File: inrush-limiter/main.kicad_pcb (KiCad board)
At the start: 2 copper layers, 27 parts, among them K1 RELAY_2RT, P1 CONN_01X04, P2 CONN_01X02, Q1 PN2222A, Q2 PN2222A, U1 LM393

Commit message: fix connections
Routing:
- net Net-(Q1-Pad2): track 0.00 -> 6.88 mm
- net GND: track 138.0 -> 138.8 mm
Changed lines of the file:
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@@
   (general
     (links 46)
-    (no_connects 2)
+    (no_connects 0)
     (area 112.645 37.775 201.022 98.675001)
     (thickness 1.6)
     (drawings 0)
-    (tracks 122)
+    (tracks 127)
     (zones 0)
     (modules 27)
@@
     (pad_to_mask_clearance 0.2)
     (aux_axis_origin 0 0)
-    (visible_elements FFFFFF7F)
+    (visible_elements FFFFFFFF)
     (pcbplotparams
       (layerselection 0x00030_80000001)
@@
   (segment (start 127 90.17) (end 133.35 90.17) (width 0.5) (layer B.Cu) (net 1))
   (segment (start 124.46 83.82) (end 124.46 87.63) (width 0.5) (layer B.Cu) (net 1) (status 30))
+  (segment (start 142.23746 67.30948) (end 147.31746 67.30948) (width 0.5) (layer B.Cu) (net 2))
+  (segment (start 121.92 58.42) (end 121.92 72.39) (width 0.5) (layer B.Cu) (net 2))
+  (segment (start 116.84 72.39) (end 116.84 76.2) (width 0.5) (layer B.Cu) (net 2))
+  (segment (start 118.11 72.39) (end 116.84 72.39) (width 0.5) (layer B.Cu) (net 2))
+  (segment (start 121.92 72.39) (end 118.11 72.39) (width 0.5) (layer B.Cu) (net 2))
   (segment (start 130.81 50.8) (end 121.93 50.8) (width 0.5) (layer B.Cu) (net 2) (status 20))
   (segment (start 130.81 60.96) (end 130.81 50.8) (width 0.5) (layer B.Cu) (net 2))
@@
   (segment (start 121.93 50.8) (end 121.92 50.79) (width 0.5) (layer B.Cu) (net 2) (status 30))
   (segment (start 121.92 50.79) (end 121.92 58.42) (width 0.5) (layer B.Cu) (net 2) (status 30))
-  (segment (start 116.84 74.93) (end 118.11 73.66) (width 0.5) (layer B.Cu) (net 2))
+  (segment (start 116.84 74.93) (end 116.84 76.2) (width 0.5) (layer B.Cu) (net 2))
   (segment (start 119.38 90.13) (end 118.07 90.13) (width 0.5) (layer B.Cu) (net 2) (status 10))
+  (segment (start 116.84 76.2) (end 116.84 88.9) (width 0.5) (layer B.Cu) (net 2))
   (segment (start 116.84 88.9) (end 118.07 90.13) (width 0.5) (layer B.Cu) (net 2))
-  (segment (start 116.84 74.93) (end 116.84 88.9) (width 0.5) (layer B.Cu) (net 2))
-  (segment (start 118.11 73.66) (end 137.16 73.66) (width 0.5) (layer B.Cu) (net 2))
   (segment (start 124.46 95.25) (end 121.92 95.25) (width 0.5) (layer B.Cu) (net 2) (status 10))
   (segment (start 121.92 95.25) (end 119.38 92.71) (width 0.5) (layer B.Cu) (net 2))
   (segment (start 119.38 92.71) (end 119.38 90.13) (width 0.5) (layer B.Cu) (net 2) (status 20))
-  (segment (start 137.16 67.31) (end 137.16 73.66) (width 0.5) (layer B.Cu) (net 2) (status 10))
   (segment (start 142.23746 67.30948) (end 137.16052 67.30948) (width 0.5) (layer B.Cu) (net 2) (status 30))
   (segment (start 137.16052 67.30948) (end 137.16 67.31) (width 0.5) (layer B.Cu) (net 2) (status 30))
@@
   (segment (start 165.1 64.77) (end 165.1 69.85) (width 2) (layer B.Cu) (net 4))
   (segment (start 165.52926 64.34074) (end 165.1 64.77) (width 2) (layer B.Cu) (net 4))
-  (segment (start 121.92 46.99) (end 119.38 49.53) (width 0.5) (layer B.Cu) (net 5) (status 400000))
-  (segment (start 119.38 49.53) (end 119.38 58.42) (width 0.5) (layer B.Cu) (net 5) (status 800000))
-  (segment (start 121.92 46.99) (end 125.73 43.18) (width 0.5) (layer B.Cu) (net 5) (status 400000))
-  (segment (start 125.73 43.18) (end 130.81 43.18) (width 0.5) (layer B.Cu) (net 5) (status 800000))
+  (segment (start 121.92 46.99) (end 119.38 49.53) (width 0.5) (layer B.Cu) (net 5) (status 10))
+  (segment (start 119.38 49.53) (end 119.38 58.42) (width 0.5) (layer B.Cu) (net 5) (status 20))
+  (segment (start 121.92 46.99) (end 125.73 43.18) (width 0.5) (layer B.Cu) (net 5) (status 10))
+  (segment (start 125.73 43.18) (end 130.81 43.18) (width 0.5) (layer B.Cu) (net 5) (status 20))
   (segment (start 137.16254 43.18052) (end 132.08052 43.18052) (width 0.5) (layer B.Cu) (net 5) (status 10))
   (segment (start 132.08052 43.18052) (end 130.81104 43.18) (width 0.5) (layer B.Cu) (net 5) (status 20))
@@
   (segment (start 147.31746 53.33948) (end 147.32 53.33694) (width 0.5) (layer B.Cu) (net 6) (status 30))
   (segment (start 147.32306 53.34) (end 147.32254 53.33948) (width 0.5) (layer B.Cu) (net 6) (status 30))
-  (segment (start 137.16254 53.34052) (end 137.16254 46.99254) (width 0.5) (layer B.Cu) (net 7) (status 400000))
-  (segment (start 135.89 45.72) (end 130.81 45.72) (width 0.5) (layer B.Cu) (net 7) (status 800000))
+  (segment (start 137.16254 53.34052) (end 137.16254 46.99254) (width 0.5) (layer B.Cu) (net 7) (status 10))
+  (segment (start 135.89 45.72) (end 130.81 45.72) (width 0.5) (layer B.Cu) (net 7) (status 20))
   (segment (start 137.16254 46.99254) (end 135.89 45.72) (width 0.5) (layer B.Cu) (net 7))
   (segment (start 137.16 53.33798) (end 137.16254 53.34052) (width 0.5) (layer B.Cu) (net 7) (status 30))
@@
   (segment (start 177.39868 69.85) (end 177.8 70.25132) (width 2) (layer B.Cu) (net 8) (status 30))
   (segment (start 178.20132 69.85) (end 177.8 70.25132) (width 2) (layer B.Cu) (net 8) (status 30))
-  (segment (start 190.5 52.23) (end 171.61 52.23) (width 2) (layer B.Cu) (net 9))
-  (segment (start 171.61 52.23) (end 170.18 50.8) (width 2) (layer B.Cu) (net 9))
+  (segment (start 190.5 52.23) (end 171.61 52.23) (width 2) (layer B.Cu) (net 9) (status 10))
+  (segment (start 171.61 52.23) (end 170.18 50.8) (width 2) (layer B.Cu) (net 9) (status 20))
   (segment (start 190.5 57.23) (end 190.5 52.23) (width 2) (layer B.Cu) (net 9) (status 30))
   (segment (start 190.5 52.23) (end 190.34 52.07) (width 2) (layer B.Cu) (net 9) (status 30))
+  (segment (start 156.21 80.01) (end 154.94 81.28) (width 0.5) (layer B.Cu) (net 10) (status 10))
+  (segment (start 154.94 81.28) (end 154.94 86.36) (width 0.5) (layer B.Cu) (net 10) (status 20))
   (segment (start 130.81 87.63) (end 130.81 83.82) (width 0.5) (layer B.Cu) (net 11) (status 30))
   (segment (start 130.81 83.82) (end 137.16 83.82) (width 0.5) (layer B.Cu) (net 11) (status 30))
@@
   (segment (start 160.02 52.07) (end 163.83 52.07) (width 0.5) (layer B.Cu) (net 17) (status 10))
   (segment (start 163.83 52.07) (end 164.86 51.04) (width 0.5) (layer B.Cu) (net 17) (status 20))
-  (segment (start 190.5 47.23) (end 190.5 46.99) (width 2) (layer B.Cu) (net 18))
-  (segment (start 190.5 46.99) (end 185.84926 42.33926) (width 2) (layer B.Cu) (net 18))
-  (segment (start 185.84926 42.33926) (end 177.8 42.33926) (width 2) (layer B.Cu) (net 18))
+  (segment (start 190.5 47.23) (end 190.5 46.99) (width 2) (layer B.Cu) (net 18) (status 30))
+  (segment (start 190.5 46.99) (end 185.84926 42.33926) (width 2) (layer B.Cu) (net 18) (status 10))
+  (segment (start 185.84926 42.33926) (end 177.8 42.33926) (width 2) (layer B.Cu) (net 18) (status 20))
   (segment (start 177.8 42.33926) (end 178.22926 42.33926) (width 2) (layer B.Cu) (net 18) (status 30))
   (zone (net 2) (net_name GND) (layer B.Cu) (hatch edge 0.508)

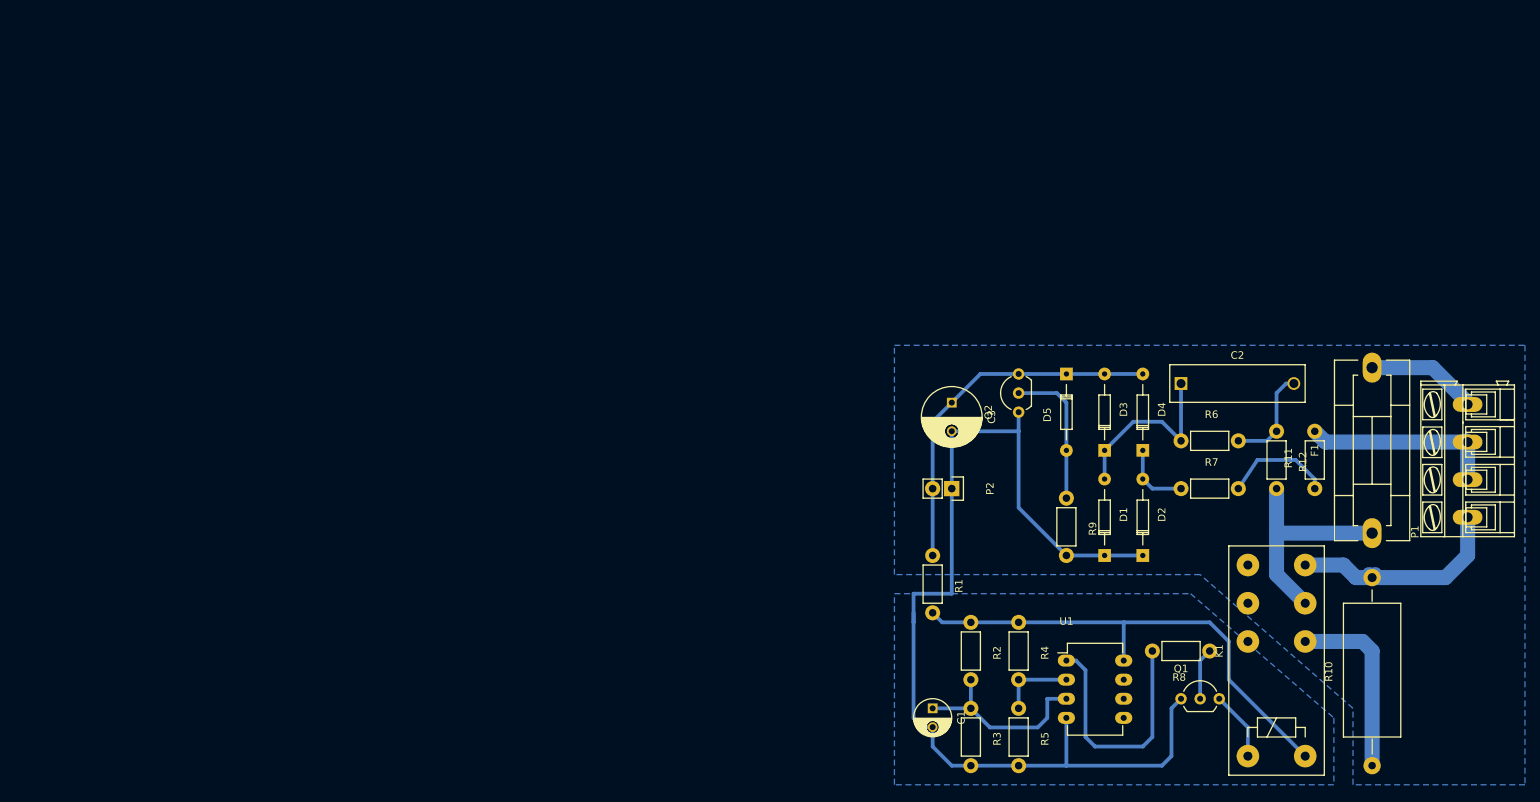
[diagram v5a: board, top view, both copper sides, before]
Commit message: add leds
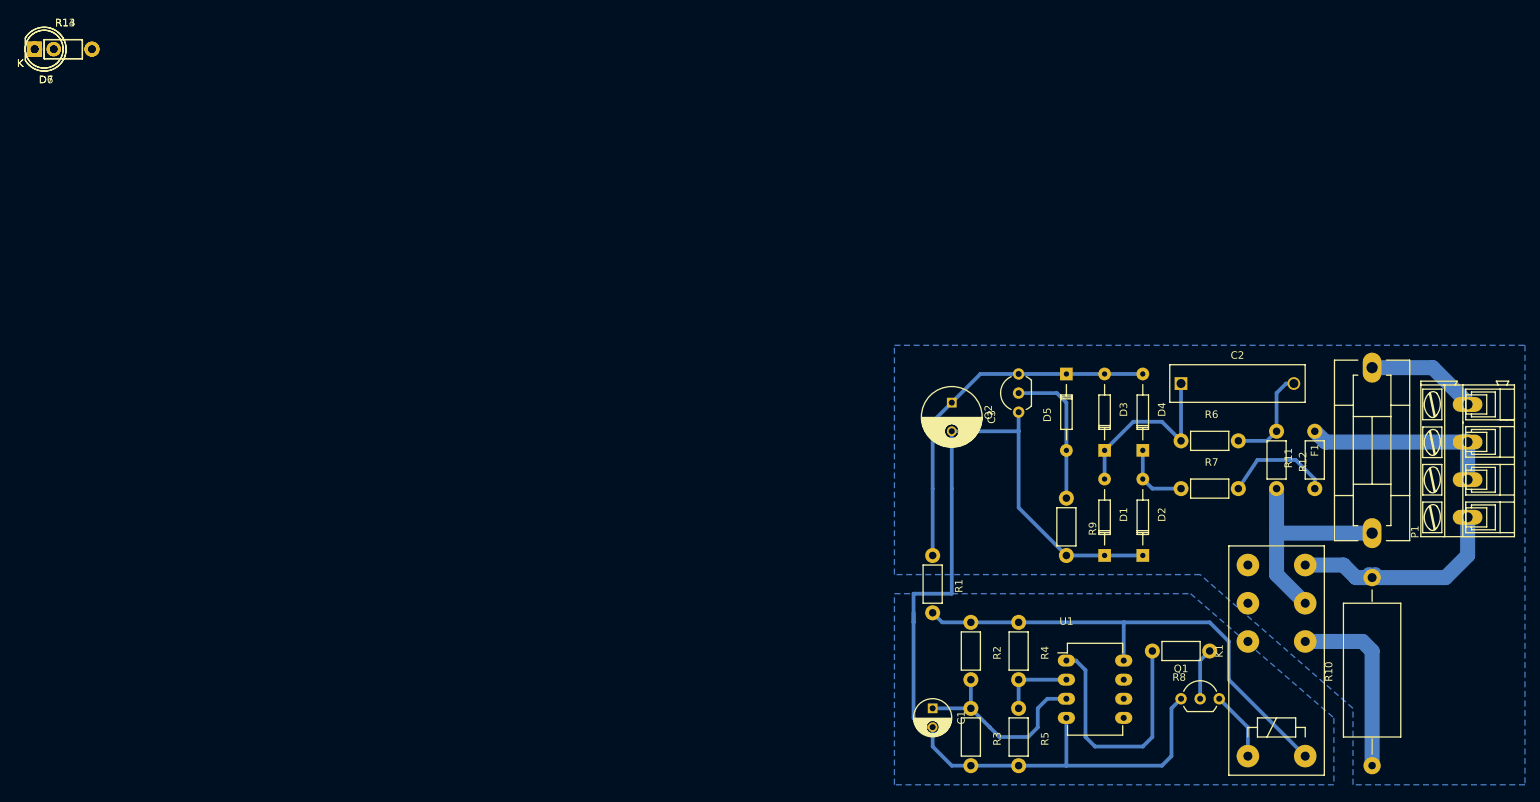
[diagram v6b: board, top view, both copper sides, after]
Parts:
- removed P2: CONN_01X02, Pin_Headers:Pin_Header_Straight_1x02
- added D6, D7: LED, LEDs:LED-5MM, F.Cu at (0.00, 0.00)
- added R13, R14: 140, Resistors_ThroughHole:Resistor_Horizontal_RM7mm, F.Cu at (0.00, 0.00)
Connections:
- C3 pad 2: GND -> Net-(C3-Pad2)
- D1 pad 1: GND -> Net-(C3-Pad2)
- D2 pad 1: GND -> Net-(C3-Pad2)
- Q2 pad 1: GND -> Net-(C3-Pad2)
- R1 pad 2: Net-(K1-PadA2) -> Net-(R1-Pad2)
- R2 pad 1: Net-(K1-PadA2) -> Net-(R1-Pad2)
- R9 pad 2: GND -> Net-(C3-Pad2)
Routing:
- net GND: track 138.8 -> 53.6 mm
- net Net-(C3-Pad2): track 0.00 -> 85.2 mm
- net Net-(R1-Pad2): track 0.00 -> 12.0 mm
- net Net-(K1-PadA2): track 65.5 -> 53.5 mm
- net Net-(C1-Pad1): track 25.7 -> 26.8 mm

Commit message: add leds
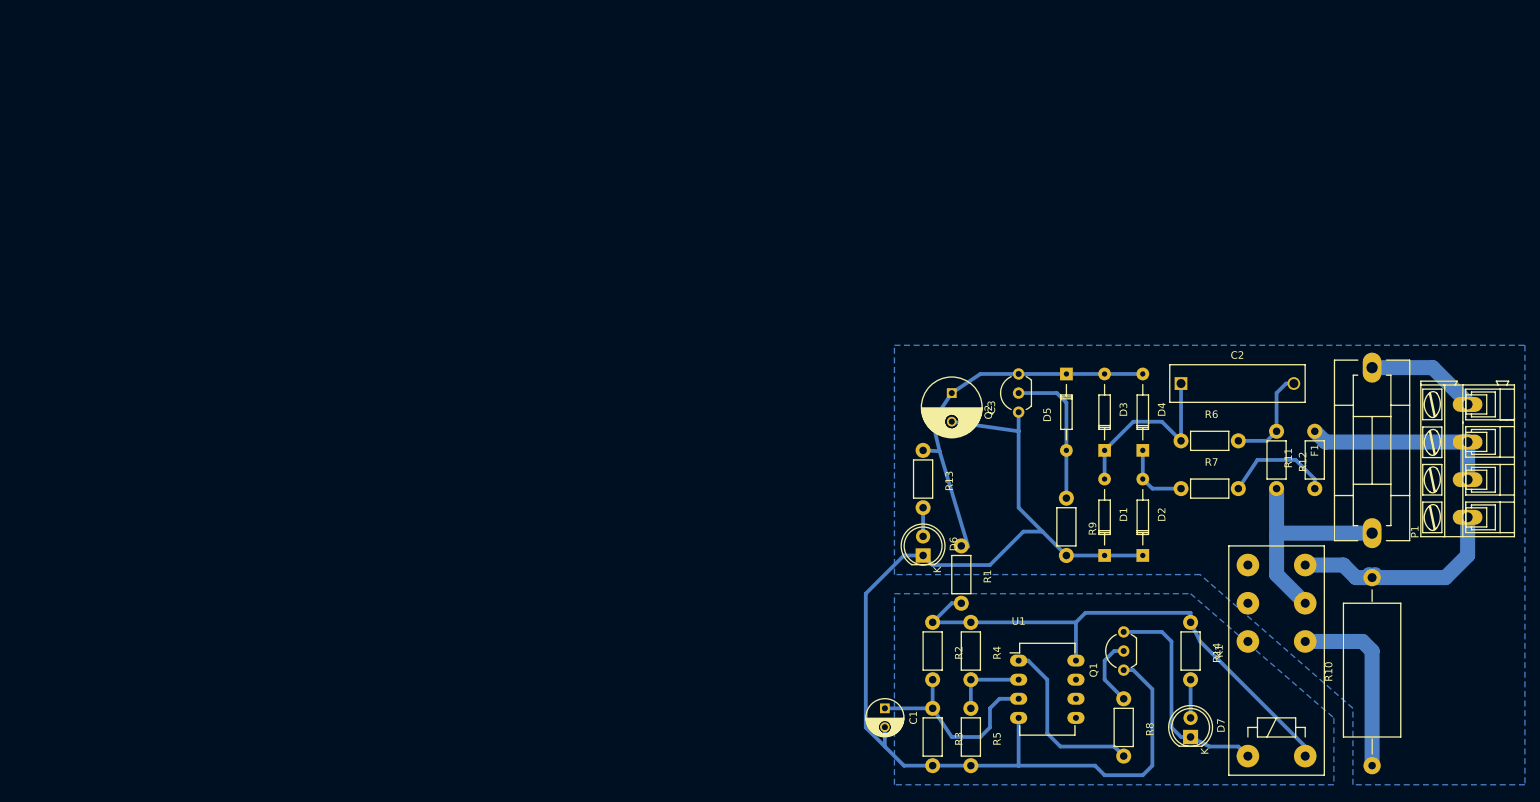
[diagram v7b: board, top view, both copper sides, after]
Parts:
- moved D7 178.8 mm to (153.7, 91.4), turned to 90 degrees
- moved R14 171.5 mm to (153.7, 76.2), turned to 270 degrees
- moved D6 135.9 mm to (118.1, 67.3), turned to 90 degrees
- moved R13 129.6 mm to (118.1, 53.3), turned to 270 degrees
- moved R8 13.1 mm to (144.8, 86.4), turned to 270 degrees
- moved Q1 8.52 mm to (144.8, 82.5), turned to 90 degrees
- moved R4 6.35 mm to (124.5, 76.2)
- moved R5 6.35 mm to (124.5, 87.6)
- moved C1 6.35 mm to (113.0, 87.6)
- moved U1 6.35 mm to (130.8, 81.3)
- moved R2 5.08 mm to (119.4, 76.2)
- moved R3 5.08 mm to (119.4, 87.6)
- moved R1 4.02 mm to (123.2, 66.0)
- moved C3 1.27 mm to (121.9, 45.7)
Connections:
- C3 pad 2: Net-(C3-Pad2) -> GND
- D1 pad 1: Net-(C3-Pad2) -> GND
- D2 pad 1: Net-(C3-Pad2) -> GND
- Q2 pad 1: Net-(C3-Pad2) -> GND
- R9 pad 2: Net-(C3-Pad2) -> GND
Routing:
- net GND: track 53.6 -> 151.9 mm
- net Net-(C3-Pad2): track 85.2 -> 0.00 mm
- net Net-(D7-Pad1): track 10.5 -> 31.1 mm
- net Net-(R8-Pad2): track 33.3 -> 23.4 mm
- net Net-(K1-PadA2): track 53.5 -> 60.0 mm
- net Net-(D7-Pad2): track 0.00 -> 5.08 mm
- net Net-(D6-Pad2): track 0.00 -> 3.81 mm
- net Net-(Q1-Pad2): track 6.88 -> 9.20 mm
- net Net-(R1-Pad2): track 12.0 -> 9.94 mm
- net +5V: track 48.3 -> 50.2 mm

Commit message: update
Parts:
- moved C1 16.9 mm to (129.5, 91.4)
- moved R3 5.24 mm to (124.5, 88.9)
- moved R5 5.24 mm to (119.4, 88.9)
- moved R2 5.24 mm to (124.5, 77.5)
- moved R4 5.24 mm to (119.4, 77.5)
- moved U1 2.54 mm to (130.8, 78.7)
- moved D7 1.27 mm to (153.7, 92.7)
- moved Q1 1.27 mm to (144.8, 83.8)
- moved R1 1.27 mm to (124.5, 66.0)
- moved R14 1.27 mm to (153.7, 77.5)
- moved R8 1.27 mm to (144.8, 87.6)
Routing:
- net Net-(C1-Pad1): track 27.2 -> 17.6 mm
- net +5V: track 50.2 -> 58.3 mm
- net Net-(R4-Pad2): track 10.2 -> 17.2 mm
- net Net-(K1-PadA2): track 60.0 -> 66.5 mm
- net Net-(R1-Pad2): track 9.94 -> 3.81 mm
- net GND: track 151.9 -> 149.7 mm
- net Net-(D7-Pad1): track 31.1 -> 29.3 mm
- net Net-(R8-Pad2): track 23.4 -> 24.5 mm
